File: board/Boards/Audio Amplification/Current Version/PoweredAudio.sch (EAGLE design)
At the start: 5 parts, among them IC1 LM386N-1

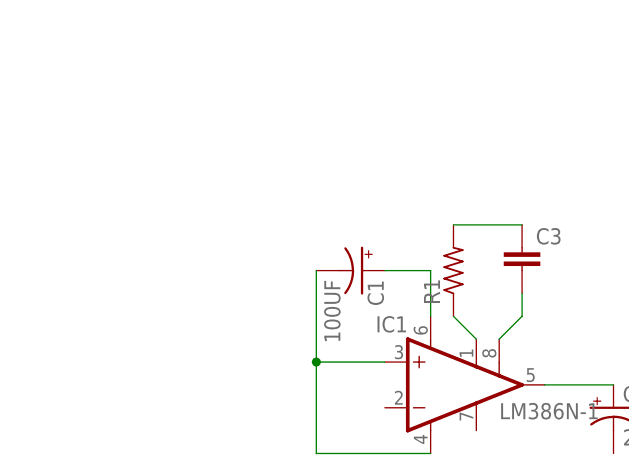
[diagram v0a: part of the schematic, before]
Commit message: changes to powered audio board
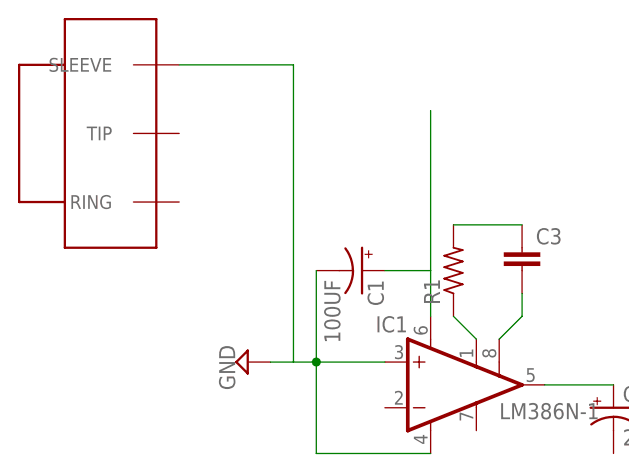
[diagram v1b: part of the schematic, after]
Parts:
- added U$1: SJ-352X, CUI SJ1-325XN:SJ-352X
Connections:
- removed net N$1: C1.-, IC1.+IN, IC1.GND
- new net GND: C1.-, IC1.+IN, IC1.GND, U$1.SLEEVE
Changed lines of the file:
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@@
 <part name="C3" library="resistor" deviceset="C-EU" device="025-025X050"/>
 <part name="R1" library="resistor" deviceset="R-US_" device="0204/5"/>
+<part name="SUPPLY1" library="supply2" deviceset="GND" device=""/>
+<part name="U$1" library="CUI SJ1-325XN" deviceset="SJ-352X" device=""/>
 </parts>
 <sheets>
@@
 <instance part="C3" gate="G$1" x="55.88" y="53.34"/>
 <instance part="R1" gate="G$1" x="48.26" y="50.8" rot="R90"/>
+<instance part="SUPPLY1" gate="GND" x="25.4" y="40.64" rot="R270"/>
+<instance part="U$1" gate="G$1" x="10.16" y="66.04" rot="R270"/>
 </instances>
 <busses>
 </busses>
 <nets>
-<net name="N$1" class="0">
-<segment>
-<pinref part="IC1" gate="G$1" pin="+IN"/>
-<wire x1="40.64" y1="40.64" x2="33.02" y2="40.64" width="0.1524" layer="91"/>
-<wire x1="33.02" y1="40.64" x2="33.02" y2="30.48" width="0.1524" layer="91"/>
-<pinref part="IC1" gate="G$1" pin="GND"/>
-<wire x1="33.02" y1="30.48" x2="45.72" y2="30.48" width="0.1524" layer="91"/>
-<pinref part="C1" gate="G$1" pin="-"/>
-<wire x1="33.02" y1="50.8" x2="33.02" y2="40.64" width="0.1524" layer="91"/>
-<junction x="33.02" y="40.64"/>
-</segment>
-</net>
 <net name="N$2" class="0">
 <segment>
@@
 <wire x1="40.64" y1="50.8" x2="45.72" y2="50.8" width="0.1524" layer="91"/>
 <wire x1="45.72" y1="50.8" x2="45.72" y2="45.72" width="0.1524" layer="91"/>
+<wire x1="45.72" y1="50.8" x2="45.72" y2="68.58" width="0.1524" layer="91"/>
 </segment>
 </net>
@@
 </segment>
 </net>
+<net name="GND" class="0">
+<segment>
+<pinref part="IC1" gate="G$1" pin="+IN"/>
+<wire x1="40.64" y1="40.64" x2="33.02" y2="40.64" width="0.1524" layer="91"/>
+<wire x1="33.02" y1="40.64" x2="33.02" y2="30.48" width="0.1524" layer="91"/>
+<pinref part="IC1" gate="G$1" pin="GND"/>
+<wire x1="33.02" y1="30.48" x2="45.72" y2="30.48" width="0.1524" layer="91"/>
+<pinref part="C1" gate="G$1" pin="-"/>
+<wire x1="33.02" y1="50.8" x2="33.02" y2="40.64" width="0.1524" layer="91"/>
+<junction x="33.02" y="40.64"/>
+<pinref part="SUPPLY1" gate="GND" pin="GND"/>
+<wire x1="27.94" y1="40.64" x2="30.48" y2="40.64" width="0.1524" layer="91"/>
+<pinref part="U$1" gate="G$1" pin="SLEEVE"/>
+<wire x1="30.48" y1="40.64" x2="33.02" y2="40.64" width="0.1524" layer="91"/>
+<wire x1="17.78" y1="73.66" x2="30.48" y2="73.66" width="0.1524" layer="91"/>
+<wire x1="30.48" y1="73.66" x2="30.48" y2="40.64" width="0.1524" layer="91"/>
+</segment>
+</net>

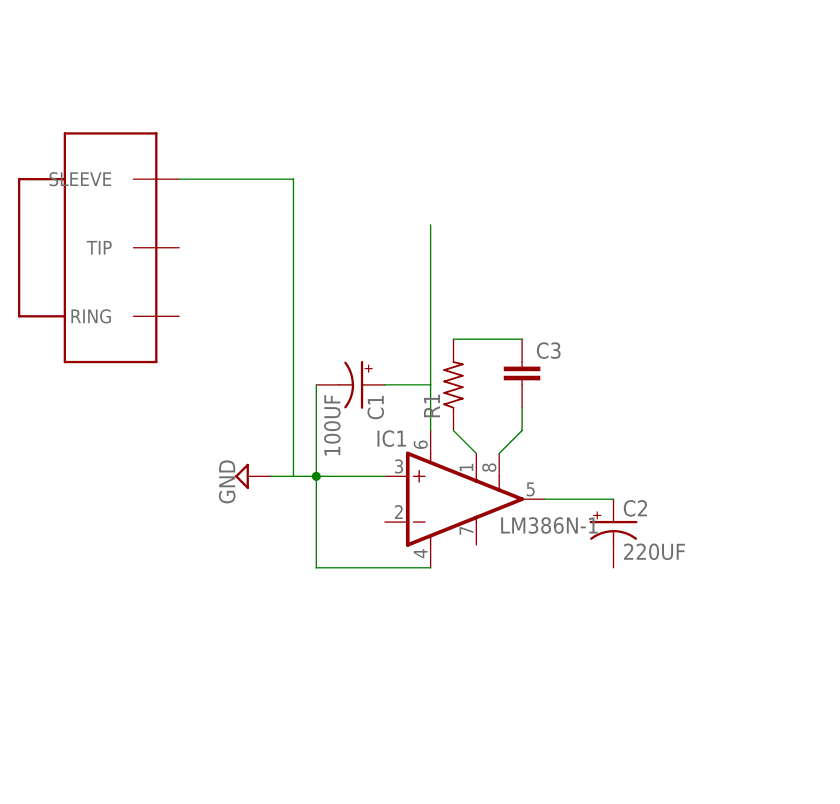
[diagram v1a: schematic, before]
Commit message: updates to the board. Added power planes
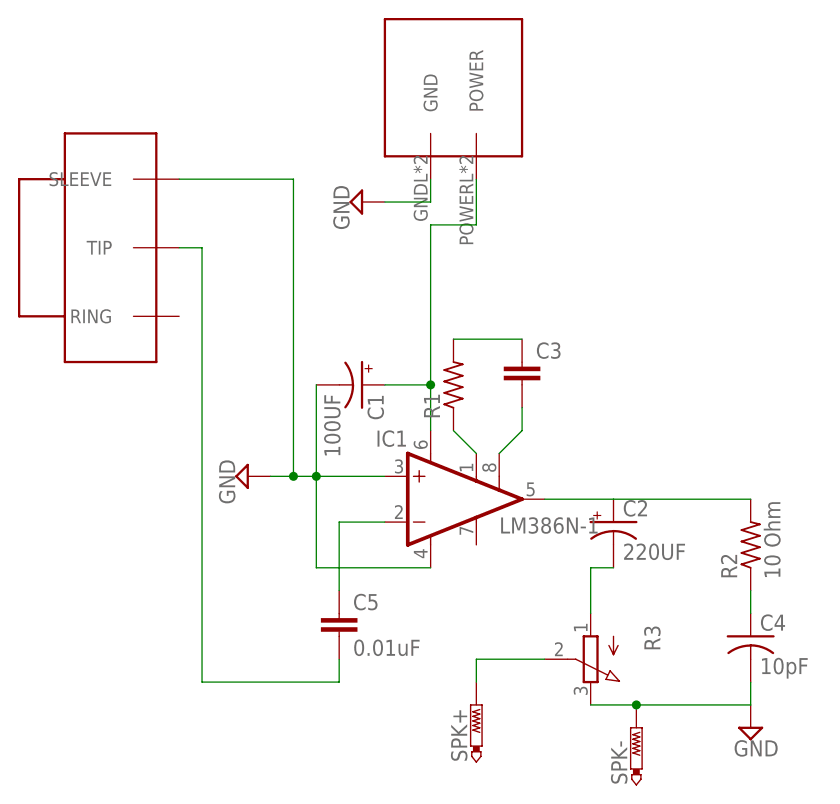
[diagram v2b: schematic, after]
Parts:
- added C4: 10pF, resistor:C-USC1206
- added C5: 0.01uF, capacitor-wima:C2.5/2
- added R2: 10 Ohm, rcl:R-US_M1206
- added R3: (no value), potModified:3RP/1610N
- added SPK+, SPK-: PTR1PAD1-13Y, testpad:PTR1PAD1-13Y
- added U$2: 2X2-MOLEX, Molex:2X2-MOLEX
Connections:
- new net N$1: C4.1, R2.1
- new net N$10: R3.S, SPK+.TP
- new net N$7: C5.1, IC1.-IN
- new net N$8: C5.2, U$1.TIP
- new net N$9: C2.-, R3.A
- net GND: now also C4.2, R3.E, SPK-.TP, U$2.GND
- net N$2: now also U$2.POWER
- net N$4: now also R2.2
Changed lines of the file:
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@@
 <part name="SUPPLY1" library="supply2" deviceset="GND" device=""/>
 <part name="U$1" library="CUI SJ1-325XN" deviceset="SJ-352X" device=""/>
+<part name="R2" library="rcl" deviceset="R-US_" device="M1206" value="10 Ohm"/>
+<part name="C4" library="resistor" deviceset="C-US" device="C1206" value="10pF"/>
+<part name="SUPPLY2" library="supply2" deviceset="GND" device=""/>
+<part name="C5" library="capacitor-wima" deviceset="C" device="2.5/2" value="0.01uF"/>
+<part name="U$2" library="Molex" deviceset="2X2-MOLEX" device=""/>
+<part name="SUPPLY3" library="supply2" deviceset="GND" device=""/>
+<part name="R3" library="potModified" deviceset="3RP/1610N" device=""/>
+<part name="SPK+" library="testpad" deviceset="PTR1" device="PAD1-13Y"/>
+<part name="SPK-" library="testpad" deviceset="PTR1" device="PAD1-13Y"/>
 </parts>
 <sheets>
@@
 <instance part="SUPPLY1" gate="GND" x="25.4" y="40.64" rot="R270"/>
 <instance part="U$1" gate="G$1" x="10.16" y="66.04" rot="R270"/>
+<instance part="R2" gate="G$1" x="81.28" y="33.02" rot="R90"/>
+<instance part="C4" gate="G$1" x="81.28" y="22.86"/>
+<instance part="SUPPLY2" gate="GND" x="81.28" y="12.7"/>
+<instance part="C5" gate="G$1" x="35.56" y="25.4"/>
+<instance part="U$2" gate="G$1" x="48.26" y="86.36" rot="R180"/>
+<instance part="SUPPLY3" gate="GND" x="38.1" y="71.12" rot="R270"/>
+<instance part="R3" gate="G$1" x="63.5" y="20.32" rot="R180"/>
+<instance part="SPK+" gate="G$1" x="50.8" y="15.24"/>
+<instance part="SPK-" gate="G$1" x="68.58" y="12.7"/>
 </instances>
 <busses>
@@
 <wire x1="45.72" y1="50.8" x2="45.72" y2="45.72" width="0.1524" layer="91"/>
 <wire x1="45.72" y1="50.8" x2="45.72" y2="68.58" width="0.1524" layer="91"/>
+<junction x="45.72" y="50.8"/>
+<pinref part="U$2" gate="G$1" pin="POWER"/>
+<wire x1="45.72" y1="68.58" x2="50.8" y2="68.58" width="0.1524" layer="91"/>
+<wire x1="50.8" y1="68.58" x2="50.8" y2="73.66" width="0.1524" layer="91"/>
 </segment>
 </net>
@@
 <pinref part="C2" gate="G$1" pin="+"/>
 <wire x1="58.42" y1="38.1" x2="66.04" y2="38.1" width="0.1524" layer="91"/>
+<pinref part="R2" gate="G$1" pin="2"/>
+<wire x1="66.04" y1="38.1" x2="81.28" y2="38.1" width="0.1524" layer="91"/>
 </segment>
 </net>
@@
 <wire x1="17.78" y1="73.66" x2="30.48" y2="73.66" width="0.1524" layer="91"/>
 <wire x1="30.48" y1="73.66" x2="30.48" y2="40.64" width="0.1524" layer="91"/>
+<junction x="30.48" y="40.64"/>
+</segment>
+<segment>
+<pinref part="SUPPLY2" gate="GND" pin="GND"/>
+<pinref part="C4" gate="G$1" pin="2"/>
+<wire x1="81.28" y1="15.24" x2="81.28" y2="17.78" width="0.1524" layer="91"/>
+<pinref part="R3" gate="G$1" pin="E"/>
+<wire x1="63.5" y1="15.24" x2="68.58" y2="15.24" width="0.1524" layer="91"/>
+<pinref part="SPK-" gate="G$1" pin="TP"/>
+<wire x1="68.58" y1="15.24" x2="81.28" y2="15.24" width="0.1524" layer="91"/>
+<junction x="68.58" y="15.24"/>
+</segment>
+<segment>
+<pinref part="SUPPLY3" gate="GND" pin="GND"/>
+<pinref part="U$2" gate="G$1" pin="GND"/>
+<wire x1="40.64" y1="71.12" x2="45.72" y2="71.12" width="0.1524" layer="91"/>
+<wire x1="45.72" y1="71.12" x2="45.72" y2="73.66" width="0.1524" layer="91"/>
 </segment>
 </net>
+<net name="N$1" class="0">
+<segment>
+<pinref part="C4" gate="G$1" pin="1"/>
+<pinref part="R2" gate="G$1" pin="1"/>
+<wire x1="81.28" y1="25.4" x2="81.28" y2="27.94" width="0.1524" layer="91"/>
+</segment>
+</net>
+<net name="N$7" class="0">
+<segment>
+<pinref part="C5" gate="G$1" pin="1"/>
+<wire x1="35.56" y1="27.94" x2="35.56" y2="35.56" width="0.1524" layer="91"/>
+<pinref part="IC1" gate="G$1" pin="-IN"/>
+<wire x1="35.56" y1="35.56" x2="40.64" y2="35.56" width="0.1524" layer="91"/>
+</segment>
+</net>
+<net name="N$8" class="0">
+<segment>
+<pinref part="U$1" gate="G$1" pin="TIP"/>
+<wire x1="17.78" y1="66.04" x2="20.32" y2="66.04" width="0.1524" layer="91"/>
+<wire x1="20.32" y1="66.04" x2="20.32" y2="17.78" width="0.1524" layer="91"/>
+<pinref part="C5" gate="G$1" pin="2"/>
+<wire x1="20.32" y1="17.78" x2="35.56" y2="17.78" width="0.1524" layer="91"/>
+<wire x1="35.56" y1="17.78" x2="35.56" y2="20.32" width="0.1524" layer="91"/>
+</segment>
+</net>
+<net name="N$9" class="0">
+<segment>
+<pinref part="C2" gate="G$1" pin="-"/>
+<pinref part="R3" gate="G$1" pin="A"/>
+<wire x1="66.04" y1="30.48" x2="63.5" y2="30.48" width="0.1524" layer="91"/>
+<wire x1="63.5" y1="30.48" x2="63.5" y2="25.4" width="0.1524" layer="91"/>
+</segment>
+</net>
+<net name="N$10" class="0">
+<segment>
+<pinref part="R3" gate="G$1" pin="S"/>
+<wire x1="58.42" y1="20.32" x2="50.8" y2="20.32" width="0.1524" layer="91"/>
+<wire x1="50.8" y1="20.32" x2="50.8" y2="17.78" width="0.1524" layer="91"/>
+<pinref part="SPK+" gate="G$1" pin="TP"/>
+</segment>
+</net>
